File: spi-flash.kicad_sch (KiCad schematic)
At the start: 49 parts, among them J23 DM3AT-SF-PEJM5, U12 MT25QL256ABA1EW7-0SIT, U13 MT25QL256ABA1EW7-0SIT, U14 MT25QL256ABA1EW7-0SIT

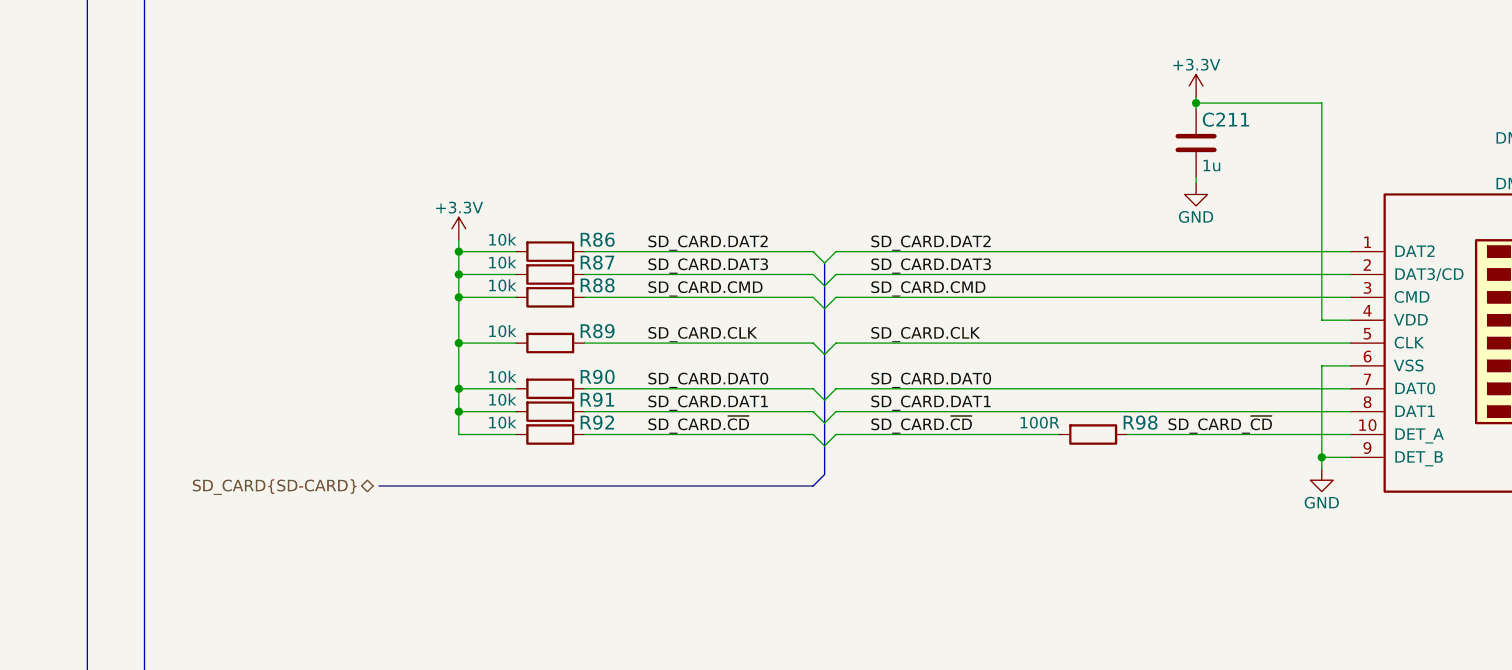
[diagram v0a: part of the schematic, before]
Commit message: Implemented fixes after schematic review
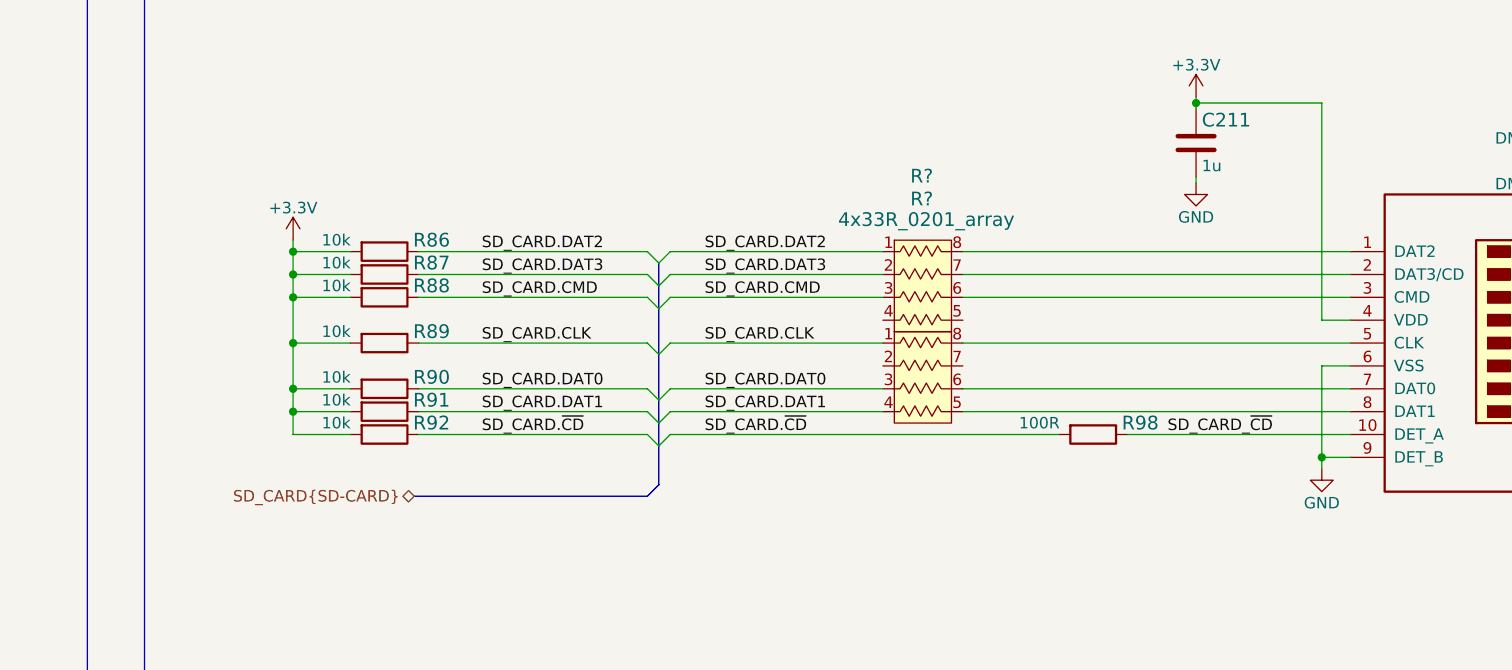
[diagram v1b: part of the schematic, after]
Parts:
- added R? (x2): 4x33R_0201_array, antmicro-footprints:EXB18V, symbol antmicroResistorNetworksArrays:4x33R_0201_array
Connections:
- net SD_CARD.CLK: now also R?.1; no longer J23.5 (CLK)
- net SD_CARD.CMD: now also R?.3; no longer J23.3 (CMD)
- net SD_CARD.DAT0: now also R?.3; no longer J23.7 (DAT0)
- net SD_CARD.DAT1: now also R?.4; no longer J23.8 (DAT1)
- net SD_CARD.DAT2: now also R?.1; no longer J23.1 (DAT2)
- net SD_CARD.DAT3: now also R?.2; no longer J23.2 (DAT3/CD)
- new net: J23.3 (CMD), R?.6
- new net: J23.2 (DAT3/CD), R?.7
- new net: J23.1 (DAT2), R?.8
- new net: J23.5 (CLK), R?.8
- new net: J23.7 (DAT0), R?.6
- new net: J23.8 (DAT1), R?.5
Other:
- moved on the sheet: R86, R87, R88, R89, R90, R91, R92

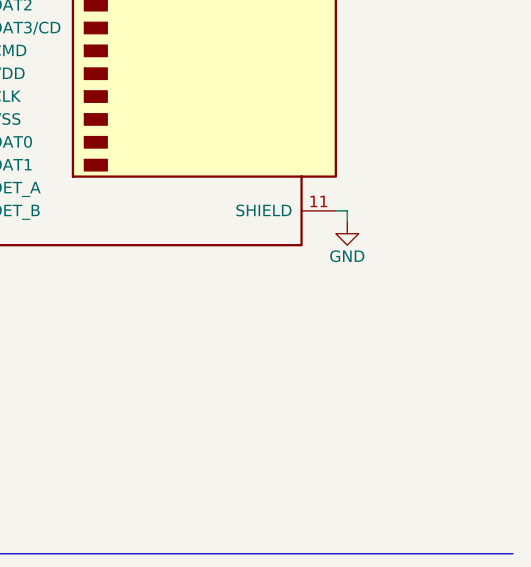
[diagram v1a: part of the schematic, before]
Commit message: Added 100n + 100R on SD card shield
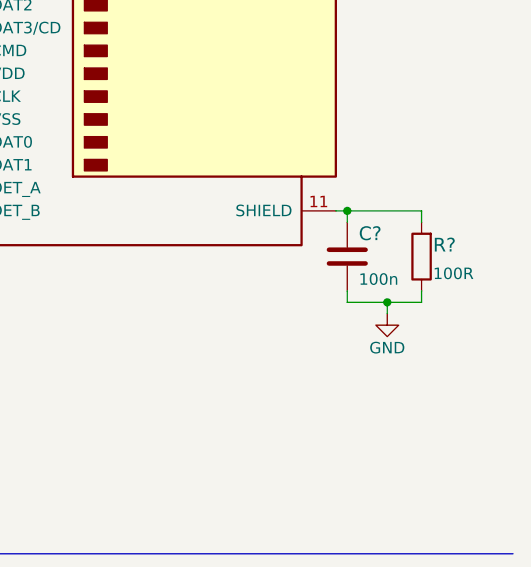
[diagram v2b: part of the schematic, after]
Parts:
- added C?: C_100n_0402, antmicro-footprints:0402-cap, symbol antmicroCapacitors0402:C_100n_0402
- added R?: R_100R_0402, antmicro-footprints:0402-res, symbol antmicroResistors0402:R_100R_0402
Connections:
- net GND: now also C?.2, R?.1; no longer J23.11 (SHIELD)
- new net: C?.1, J23.11 (SHIELD), R?.2

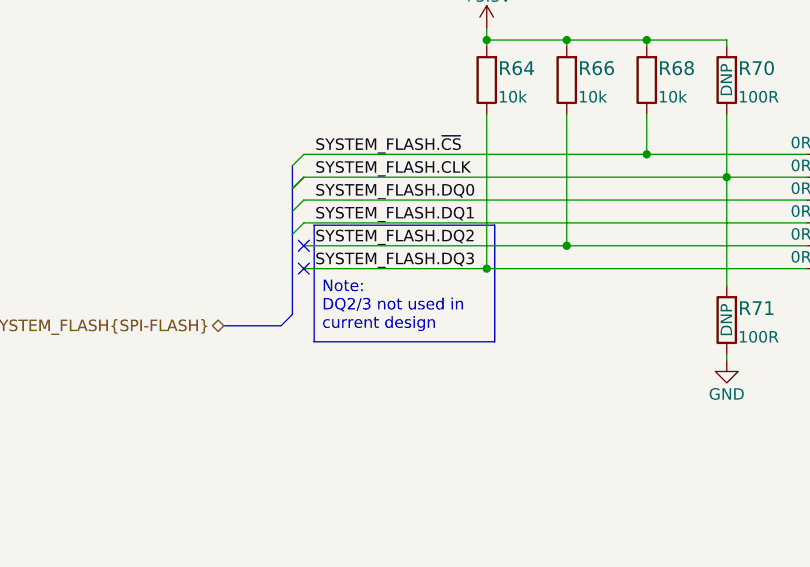
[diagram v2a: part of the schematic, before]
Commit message: Connected DQ2 DQ3 lines of SPI flash to FPGA bank 14
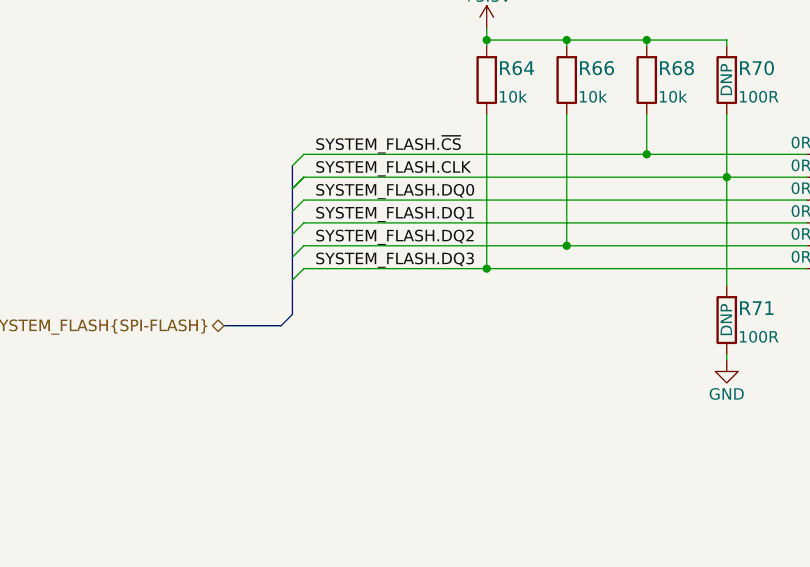
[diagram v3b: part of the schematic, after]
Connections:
- no-connect marks 2 -> 0
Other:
- note removed: "Note: DQ2/3 not used in current design"
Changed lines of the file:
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@@
   (junction (at 387.985 88.9) (diameter 0) (color 0 0 0 0)
   )
-  (no_connect (at 53.975 76.2))
-  (no_connect (at 53.975 78.74))
   (bus_entry (at 52.705 69.85) (size 1.27 -1.27)
     (stroke (width 0) (type default) (color 0 0 0 0))
@@
     (stroke (width 0) (type default) (color 0 0 0 0))
   )
+  (bus_entry (at 52.705 77.47) (size 1.27 -1.27)
+    (stroke (width 0) (type default) (color 0 0 0 0))
+  )
   (bus_entry (at 52.705 193.04) (size 1.27 -1.27)
     (stroke (width 0) (type default) (color 0 0 0 0))
@@
     (stroke (width 0) (type default) (color 0 0 0 0))
   )
+  (bus_entry (at 52.705 80.01) (size 1.27 -1.27)
+    (stroke (width 0) (type default) (color 0 0 0 0))
+  )
   (bus_entry (at 52.705 200.66) (size 1.27 -1.27)
     (stroke (width 0) (type default) (color 0 0 0 0))
@@
     (stroke (width 0) (type default) (color 0 0 0 0))
   )
+  (bus (pts (xy 52.705 77.47) (xy 52.705 80.01))
+    (stroke (width 0) (type default) (color 0 0 0 0))
+  )
   (wire (pts (xy 392.43 99.06) (xy 387.985 99.06))
     (stroke (width 0) (type default) (color 0 0 0 0))
@@
     (stroke (width 0) (type default) (color 0 0 0 0))
   )
-  (polyline (pts (xy 55.118 73.914) (xy 75.184 73.914))
-    (stroke (width 0) (type default) (color 0 0 0 0))
-  )
   (wire (pts (xy 265.43 71.12) (xy 240.03 71.12))
     (stroke (width 0) (type default) (color 0 0 0 0))
@@
     (stroke (width 0) (type default) (color 0 0 0 0))
   )
-  (bus (pts (xy 52.705 74.93) (xy 52.705 83.82))
+  (bus (pts (xy 52.705 74.93) (xy 52.705 77.47))
     (stroke (width 0) (type default) (color 0 0 0 0))
   )
@@
     (stroke (width 0) (type default) (color 0 0 0 0))
   )
+  (bus (pts (xy 52.705 80.01) (xy 52.705 83.82))
+    (stroke (width 0) (type default) (color 0 0 0 0))
+  )
   (wire (pts (xy 175.26 199.39) (xy 173.99 199.39))
     (stroke (width 0) (type default) (color 0 0 0 0))
@@
     (stroke (width 0) (type default) (color 0 0 0 0))
   )
-  (polyline (pts (xy 75.184 73.914) (xy 75.184 86.868))
-    (stroke (width 0) (type default) (color 0 0 0 0))
-  )
   (wire (pts (xy 232.41 68.58) (xy 226.06 68.58))
     (stroke (width 0) (type default) (color 0 0 0 0))
@@
     (stroke (width 0) (type default) (color 0 0 0 0))
   )
-  (polyline (pts (xy 75.184 86.868) (xy 55.118 86.868))
-    (stroke (width 0) (type default) (color 0 0 0 0))
-  )
   (wire (pts (xy 53.975 71.12) (xy 109.855 71.12))
     (stroke (width 0) (type default) (color 0 0 0 0))
@@
   )
   (wire (pts (xy 387.985 88.9) (xy 396.24 88.9))
-    (stroke (width 0) (type default) (color 0 0 0 0))
-  )
-  (polyline (pts (xy 55.118 73.914) (xy 55.118 86.868))
     (stroke (width 0) (type default) (color 0 0 0 0))
   )
@@
     (effects (font (size 2 2) (thickness 0.5994) bold) (justify left bottom))
   )
-  (text "Note:\nDQ2/3 not used in \ncurrent design" (at 56.007 85.725 0)
-    (effects (font (size 1.27 1.27)) (justify left bottom))
-  )
   (text "Follows Figure 2-14 7 Series FPGAs Configuration User Guide\nUG470 (v1.15)"

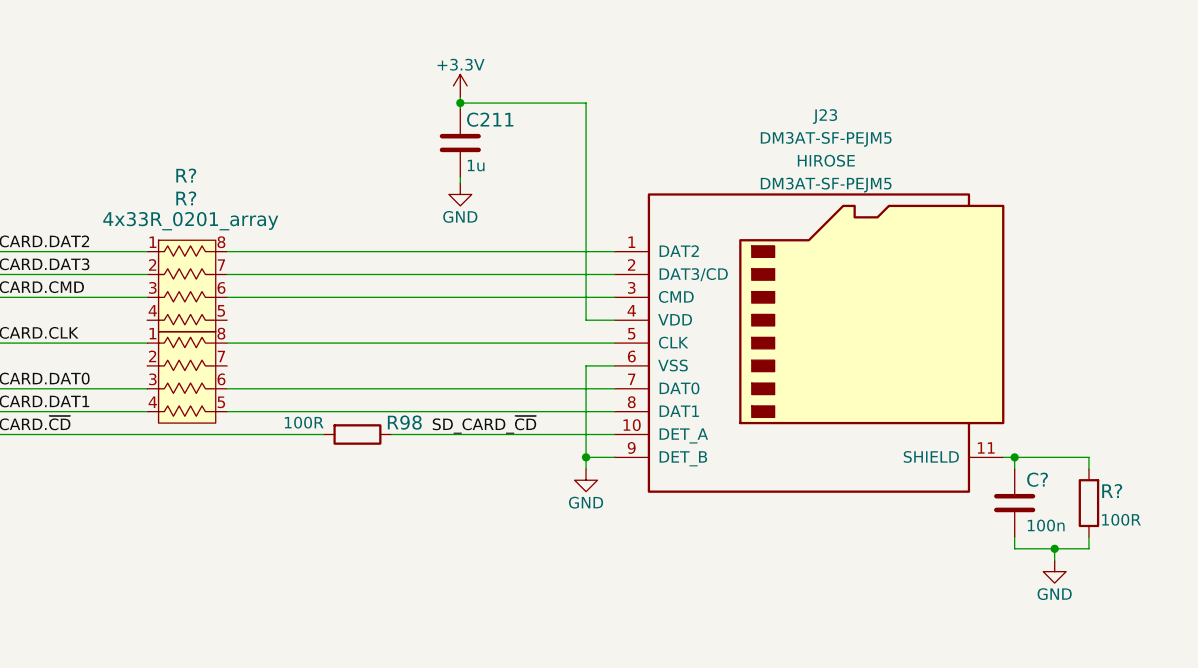
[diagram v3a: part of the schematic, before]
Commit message: Import changes to PCB. Align part of the designators
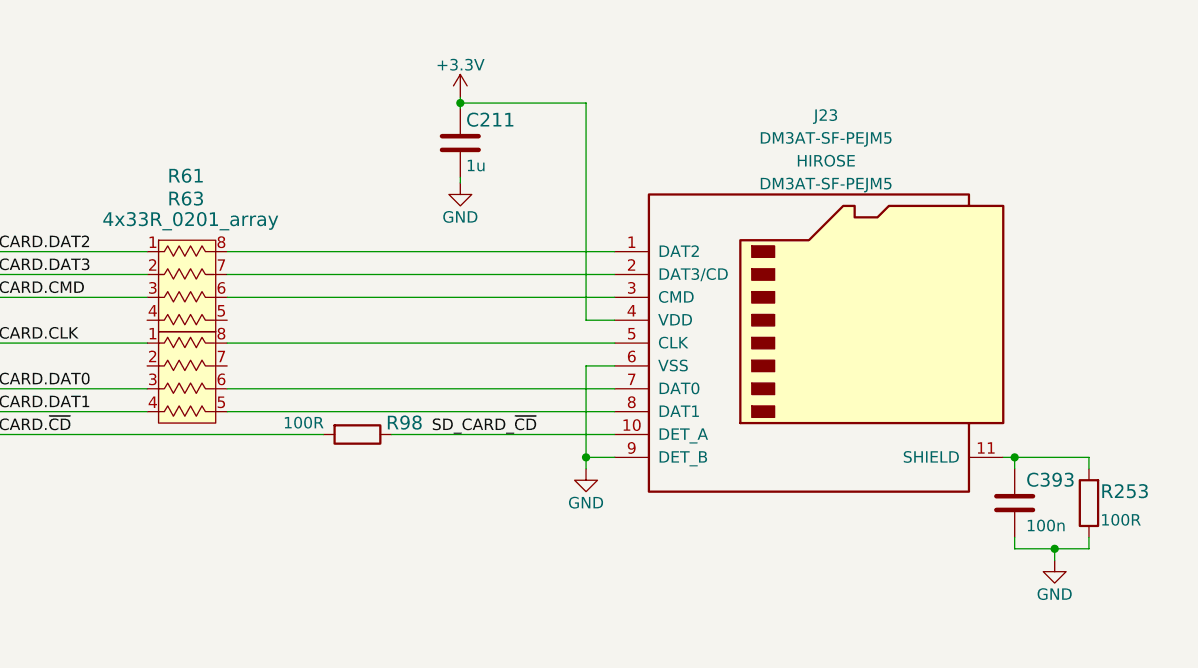
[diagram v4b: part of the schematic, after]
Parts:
- gave numbers to parts that had none: 4
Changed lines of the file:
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@@
   (symbol (lib_id "antmicroCapacitors0402:C_100n_0402") (at 387.985 93.98 0) (unit 1)
     (in_bom yes) (on_board yes)
-    (property "Reference" "C?" (id 0) (at 389.255 91.44 0)
+    (property "Reference" "C393" (id 0) (at 389.255 91.44 0)
       (effects (font (size 1.524 1.524)) (justify left))
     )
@@
   (symbol (lib_id "power:GND") (at 392.43 100.33 0) (unit 1)
     (in_bom yes) (on_board yes)
-    (property "Reference" "#PWR?" (id 0) (at 392.43 106.68 0)
+    (property "Reference" "#PWR0105" (id 0) (at 392.43 106.68 0)
       (effects (font (size 1.27 1.27)) hide)
     )
@@
   (symbol (lib_id "antmicroResistorNetworksArrays:4x33R_0201_array") (at 296.672 76.2 0) (unit 1)
     (in_bom yes) (on_board yes)
-    (property "Reference" "R?" (id 0) (at 295.91 57.658 0)
+    (property "Reference" "R61" (id 0) (at 295.91 57.658 0)
       (effects (font (size 1.524 1.524)))
     )
@@
   (symbol (lib_id "antmicroResistors0402:R_100R_0402") (at 396.24 93.98 90) (unit 1)
     (in_bom yes) (on_board yes)
-    (property "Reference" "R?" (id 0) (at 397.51 92.71 90)
+    (property "Reference" "R253" (id 0) (at 397.51 92.71 90)
       (effects (font (size 1.524 1.524)) (justify right))
     )
@@
   (symbol (lib_id "antmicroResistorNetworksArrays:4x33R_0201_array") (at 296.672 86.36 0) (unit 1)
     (in_bom yes) (on_board yes)
-    (property "Reference" "R?" (id 0) (at 295.91 60.198 0)
+    (property "Reference" "R63" (id 0) (at 295.91 60.198 0)
       (effects (font (size 1.524 1.524)))
     )

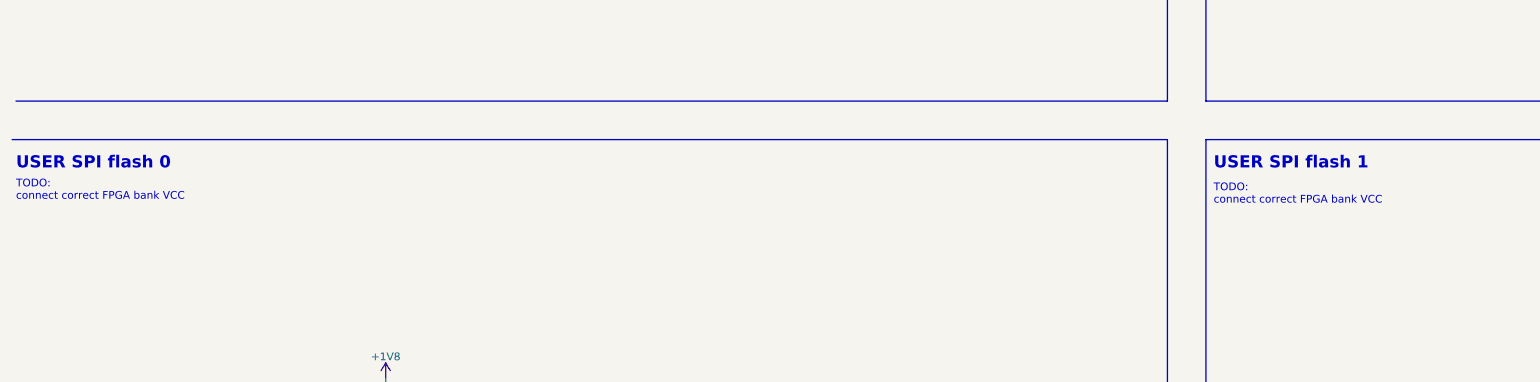
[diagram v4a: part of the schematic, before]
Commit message: Removed ToDo notes which are already done, corrected USB DET and PEN signal mapping on FPGA side, connected 200MHz generator ENA signal to FPGA
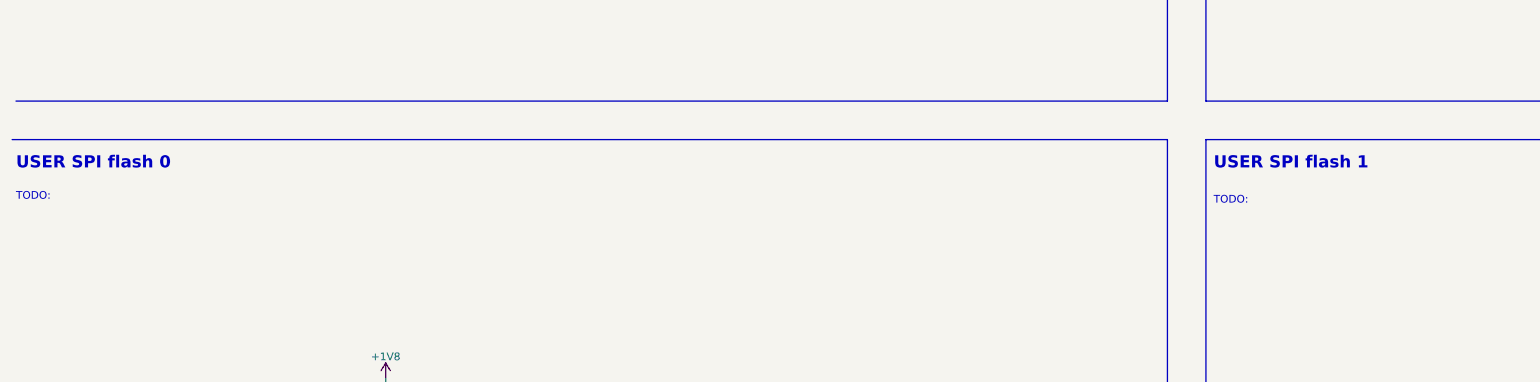
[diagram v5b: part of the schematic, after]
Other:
- note added: "TODO:"
- note removed: "TODO: connect correct FPGA bank VCC"
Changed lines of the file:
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@@
     (effects (font (size 1.5 1.5) (thickness 0.5994) bold) (justify left bottom))
   )
-  (text "TODO:\nconnect correct FPGA bank VCC" (at 210.82 144.145 0)
+  (text "TODO:" (at 210.82 144.145 0)
     (effects (font (size 1.27 1.27)) (justify left bottom))
   )
@@
     (effects (font (size 2 2) (thickness 0.5994) bold) (justify left bottom))
   )
-  (text "TODO:\nconnect correct FPGA bank VCC" (at 13.335 143.51 0)
+  (text "TODO:" (at 13.335 143.51 0)
     (effects (font (size 1.27 1.27)) (justify left bottom))
   )

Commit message: Loclib
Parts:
- C209, C210, C212, C393: footprint antmicro-footprints:0402-cap -> K410T-devboard-footprints:0402-cap; symbol antmicroCapacitors0402:C_100n_0402 -> K410T-devboard:C_100n_0402
- C211: footprint antmicro-footprints:0402-cap -> K410T-devboard-footprints:0402-cap; symbol antmicroCapacitors0402:C_1u_0402 -> K410T-devboard:C_1u_0402
- J23: footprint antmicro-footprints:MicroSD_DM3AT-SF-PEJM5 -> K410T-devboard-footprints:MicroSD_DM3AT-SF-PEJM5; symbol antmicroMemoryConnectorsPCCardSockets:DM3AT-SF-PEJM5 -> K410T-devboard:DM3AT-SF-PEJM5
- R100, R101, R102, R103, R104, R74, R75, R76, R77, R78, R79, R80, R81, R82, R83, R84, R85, R99: footprint antmicro-footprints:0402-res -> K410T-devboard-footprints:0402-res; symbol antmicroResistors0402:R_0R_0402 -> K410T-devboard:R_0R_0402
- R253, R70, R71, R72, R73, R96, R97, R98: footprint antmicro-footprints:0402-res -> K410T-devboard-footprints:0402-res; symbol antmicroResistors0402:R_100R_0402 -> K410T-devboard:R_100R_0402
- R61, R63: footprint antmicro-footprints:EXB18V -> K410T-devboard-footprints:EXB18V; symbol antmicroResistorNetworksArrays:4x33R_0201_array -> K410T-devboard:4x33R_0201_array
- R64, R65, R66, R67, R68, R69, R86, R87, R88, R89, R90, R91, R92, R93, R94, R95: footprint antmicro-footprints:0402-res -> K410T-devboard-footprints:0402-res; symbol antmicroResistors0402:R_10k_0402 -> K410T-devboard:R_10k_0402
- U12, U13, U14: footprint antmicro-footprints:WDFN-8-1EP_6x5mm_P1.27mm_EP3.4x4mm -> K410T-devboard-footprints:WDFN-8-1EP_6x5mm_P1.27mm_EP3.4x4mm; symbol antmicroMemory:MT25QL256ABA1EW7-0SIT -> K410T-devboard:MT25QL256ABA1EW7-0SIT
